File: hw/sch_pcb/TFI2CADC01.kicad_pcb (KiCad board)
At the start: 2 copper layers, 30 x 20 mm, 32 parts, among them J1 SM04B-GHS-TB, J2 SM04B-GHS-TB, J3 SM04B-GHS-TB, J4 SM04B-GHS-TB, J5 SM04B-GHS-TB, J6 SM04B-GHS-TB, U1 MIC5504-3.3YM5, U2 LTC4317

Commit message: Hotové schéma - otázka jumpery a konektory na vstupu
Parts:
- removed G1: LOGO, MLAB_LOGA:TF 10x4,7
- removed J6: SM04B-GHS-TB, Connector_JST:JST_GH_SM04B-GHS-TB_1x04-1MP_P1.25mm_Horizontal
- removed R10, R12, R15: 1M, Resistor_SMD:R_0603_1608Metric
- removed R13, R14, R9: 887k, Resistor_SMD:R_0603_1608Metric
- removed R16, R17: 10k, Resistor_SMD:R_0603_1608Metric
- removed R7: -, Resistor_SMD:R_0603_1608Metric
- removed R8: 180R, Resistor_SMD:R_0603_1608Metric
- removed U2: LTC4317, Package_DFN_QFN:DFN-16-1EP_3x5mm_P0.5mm_EP1.66x4.4mm
- added C5: 100nF, Capacitor_SMD:C_0603_1608Metric, F.Cu at (89.6, 104.2)
- added D3: LED RED, LED_SMD:LED_0603_1608Metric, F.Cu at (93.7, 111.0)
- added JP3: 0x4A, Jumper:SolderJumper-2_P1.3mm_Open_RoundedPad1.0x1.5mm, F.Cu at (85.4, 109.3)
- added JP4: 0x4B, Jumper:SolderJumper-2_P1.3mm_Open_RoundedPad1.0x1.5mm, F.Cu at (85.4, 112.9)
- added Q1: BC817, Package_TO_SOT_SMD:SOT-23, F.Cu at (94.1, 107.5)
- added R4: 10k, Resistor_SMD:R_0603_1608Metric, F.Cu at (89.6, 106.7)
- added U3: ADS1115IDGS, Package_SO:TSSOP-10_3x3mm_P0.5mm, F.Cu at (103.0, 108.2)
- C1, C2, C3, D1, D2, J3, R1, R2, R3, R5, U1: moved to F.Cu
- C4: value 100nF -> 10uF; moved to F.Cu
- J1: value SM04B-GHS-TB -> Screw_Terminal_01x06; footprint Connector_JST:JST_GH_SM04B-GHS-TB_1x04-1MP_P1.25mm_Horizontal -> TerminalBlock_Phoenix:TerminalBlock_Phoenix_PTSM-0,5-5-2,5-V-SMD_1x05-1MP_P2.50mm_Vertical; moved to F.Cu
- J2: value SM04B-GHS-TB -> ALERT/RDY; footprint Connector_JST:JST_GH_SM04B-GHS-TB_1x04-1MP_P1.25mm_Horizontal -> TestPoint:TestPoint_Keystone_5015_Micro_Mini; moved to F.Cu
- J5: value SM04B-GHS-TB -> Conn_01x06_Pin; footprint Connector_JST:JST_GH_SM04B-GHS-TB_1x04-1MP_P1.25mm_Horizontal -> Connector_PinHeader_2.54mm:PinHeader_1x06_P2.54mm_Horizontal; moved to F.Cu
- JP1: value SolderJumper_2_Open -> 0x48
- JP2: value SolderJumper_2_Open -> 0x49
- R6: value 10k -> 180R; moved to F.Cu
- moved C2 60.8 mm to (93.4, 80.6)
- moved C3 58.6 mm to (93.4, 83.1)
- moved JP1 57.6 mm to (85.4, 102.2), turned to 0 degrees
- moved JP2 57.6 mm to (85.4, 105.8), turned to 0 degrees
- moved R5 56.4 mm to (89.6, 109.2), turned to 0 degrees
- moved C4 55.1 mm to (89.6, 101.7), turned to 0 degrees
- moved R6 54.8 mm to (89.6, 111.7), turned to 0 degrees
- moved R1 50.2 mm to (93.4, 85.6), turned to 0 degrees
- moved R2 46.4 mm to (93.4, 88.1), turned to 0 degrees
- moved U1 46.1 mm to (96.4, 98.5), turned to 0 degrees
- moved D2 45.9 mm to (101.7, 80.7), turned to 0 degrees
- moved R3 44.3 mm to (93.4, 90.6), turned to 0 degrees
- moved J1 40.4 mm to (171.8, 105.0)
- moved J3 35.8 mm to (117.5, 94.0)
- moved J2 30.5 mm to (101.2, 102.3), turned to 0 degrees
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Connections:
- J1 pad 1: +5V -> unconnected-(J1-Pin_1-Pad1)
- J1 pad 2: /SCLin -> unconnected-(J1-Pin_2-Pad2)
- J1 pad 3: /SDAin -> unconnected-(J1-Pin_3-Pad3)
- J1 pad 4: GND -> unconnected-(J1-Pin_4-Pad4)
- J1 pad MP: GND -> (no net)
- J2 pad 1: +5V -> /ALERT/RDY
- J3 pad 2: /SCLout1 -> /SCL
- J3 pad 3: /SDAout1 -> /SDA
- J4 pad 2: /SCLout1 -> /SCL
- J4 pad 3: /SDAout1 -> /SDA
- J5 pad 1: +5V -> GND
- J5 pad 2: /SCLout2 -> /AIN3
- J5 pad 3: /SDAout2 -> /AIN2
- J5 pad 4: GND -> /AIN1
- JP1 pad 1: /XORL1 -> /ADDR
- JP1 pad 2: +3V3 -> GND
- JP2 pad 1: /XORL2 -> /ADDR
- R2 pad 2: /SCLin -> /SCL
- R3 pad 2: /SDAin -> /SDA
- R5 pad 1: +3V3 -> Net-(Q1-B)
- R5 pad 2: /SCLout1 -> /ALERT/RDY
- R6 pad 1: +3V3 -> +5V
- R6 pad 2: /SDAout1 -> Net-(D3-A)
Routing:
- net +5V: track 61.4 -> 0.00 mm, vias 3 -> 0
- net +3V3: track 56.3 -> 0.00 mm, vias 5 -> 0
- net /SDAin: track 22.5 -> 0.00 mm, vias 2 -> 0
- net /SCLin: track 20.5 -> 0.00 mm, vias 3 -> 0
- net /SCLout2: track 18.5 -> 0.00 mm, vias 3 -> 0
- net /SDAout2: track 18.1 -> 0.00 mm, vias 1 -> 0
- net /XORL1: track 17.4 -> 0.00 mm, vias 1 -> 0
- net /SDAout1: track 17.4 -> 0.00 mm, vias 1 -> 0
- net /SCLout1: track 16.2 -> 0.00 mm, vias 3 -> 0
- net /XORL2: track 12.4 -> 0.00 mm, vias 1 -> 0
- net /XORH1: track 9.16 -> 0.00 mm
- net /XORH2: track 6.98 -> 0.00 mm
- net GND: track 3.96 -> 0.00 mm, vias 26 -> 0
- net Net-(D1-A): track 2.50 -> 0.00 mm
- removed copper zone on B.Cu, net GND
- removed copper zone on F.Cu, net GND
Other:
- board size 30 x 20 mm -> 35 x 20 mm
- board text removed: "0x08 0x0f"
- board text removed: "0x78 0x7f"
- board text removed: "2023"
- board text removed: "I2C input (pass-trough)"
- board text removed: "OUT1"
- board text removed: "OUT2"
- board text removed: "TFI2CADT01B"
- board text removed: "thunderfly.cz"

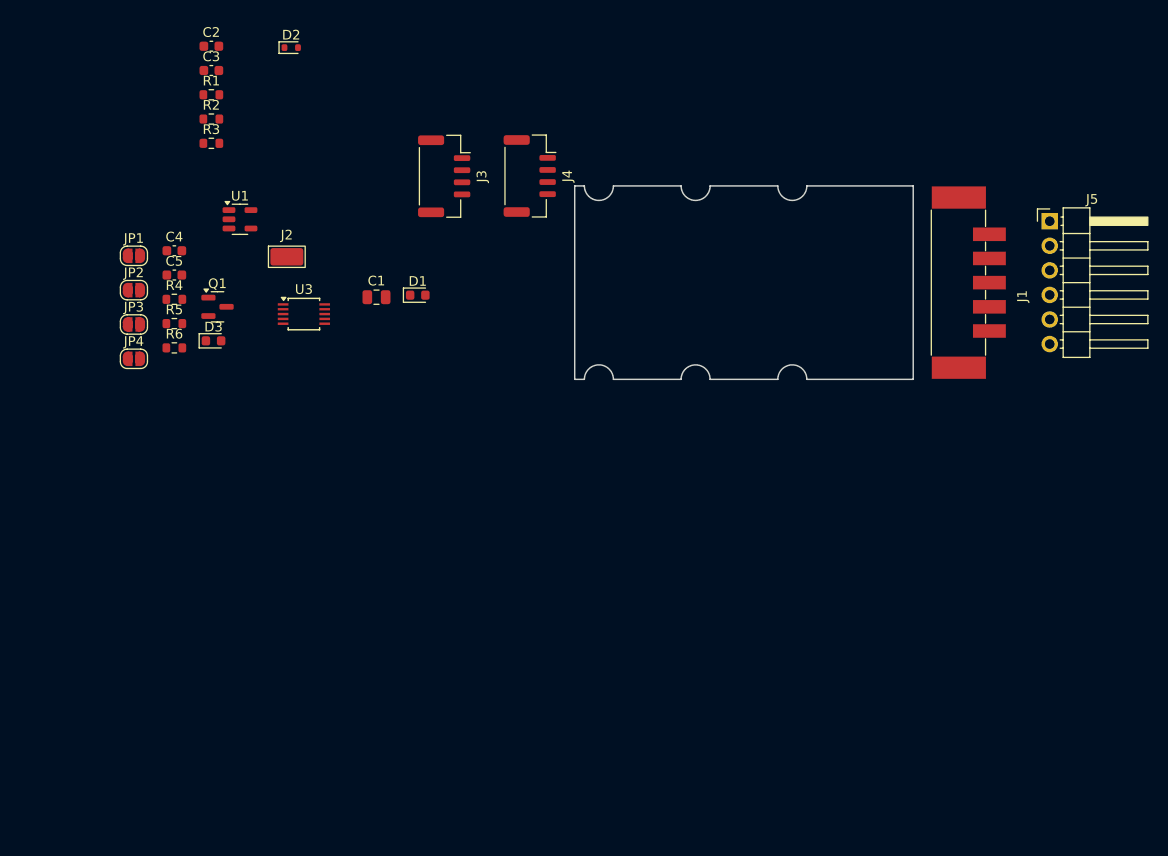
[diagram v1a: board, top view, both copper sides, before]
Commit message: ADS1115 obvod s headry
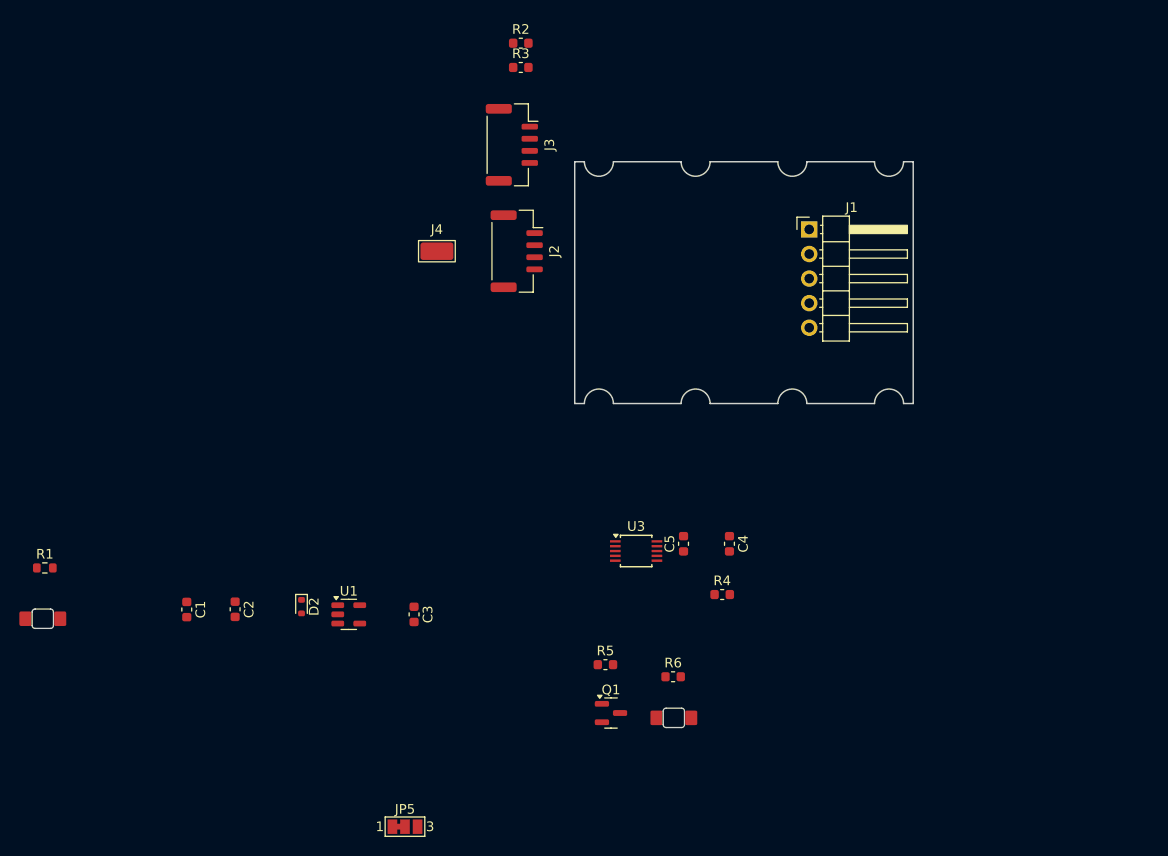
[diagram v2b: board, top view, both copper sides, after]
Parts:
- removed J5: Conn_01x06_Pin, Connector_PinHeader_2.54mm:PinHeader_1x06_P2.54mm_Horizontal
- removed JP1: 0x48, Jumper:SolderJumper-2_P1.3mm_Open_RoundedPad1.0x1.5mm
- removed JP2: 0x49, Jumper:SolderJumper-2_P1.3mm_Open_RoundedPad1.0x1.5mm
- removed JP3: 0x4A, Jumper:SolderJumper-2_P1.3mm_Open_RoundedPad1.0x1.5mm
- removed JP4: 0x4B, Jumper:SolderJumper-2_P1.3mm_Open_RoundedPad1.0x1.5mm
- added JP5: AddresSelect, Jumper:SolderJumper-3_P1.3mm_Bridged12_Pad1.0x1.5mm_NumberLabels, F.Cu at (113.5, 161.2)
- C1: footprint Capacitor_SMD:C_0805_2012Metric -> Mlab_R:SMD-0603
- C2, C3, C4, C5: footprint Capacitor_SMD:C_0603_1608Metric -> Mlab_R:SMD-0603
- D1, D3: footprint LED_SMD:LED_0603_1608Metric -> Mlab_D:LED_1206_mill
- J1: value Screw_Terminal_01x06 -> Conn_01x05_Pin; footprint TerminalBlock_Phoenix:TerminalBlock_Phoenix_PTSM-0,5-5-2,5-V-SMD_1x05-1MP_P2.50mm_Vertical -> Connector_PinHeader_2.54mm:PinHeader_1x05_P2.54mm_Horizontal
- R2, R3, R4, R5, R6: footprint Resistor_SMD:R_0603_1608Metric -> Mlab_R:SMD-0603
- moved C4 64.9 mm to (147.0, 132.0), turned to -90 degrees
- moved R4 64.3 mm to (146.2, 137.2)
- moved R6 61.8 mm to (141.2, 145.8)
- moved D3 61.5 mm to (141.2, 150.0)
- moved C3 60.0 mm to (114.4, 139.3), turned to -90 degrees
- moved C5 59.5 mm to (142.2, 132.0), turned to 90 degrees
- moved Q1 58.5 mm to (134.8, 149.5)
- moved C2 58.3 mm to (95.9, 138.8), turned to -90 degrees
- moved D2 57.8 mm to (102.8, 138.5), turned to -90 degrees
- moved R5 56.8 mm to (134.2, 144.5)
- moved R1 51.9 mm to (76.2, 134.5)
- moved D1 51.2 mm to (76.0, 139.8)
- moved U1 42.4 mm to (107.6, 139.3)
- moved U3 42.2 mm to (137.3, 132.8)
- moved C1 37.8 mm to (90.9, 138.8), turned to -90 degrees
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- renumbered J3 to J2, J4 to J3, J2 to J4
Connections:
- J1 pad 1: unconnected-(J1-Pin_1-Pad1) -> GND
- J1 pad 2: unconnected-(J1-Pin_2-Pad2) -> /AIN3
- J1 pad 3: unconnected-(J1-Pin_3-Pad3) -> /AIN2
- J1 pad 4: unconnected-(J1-Pin_4-Pad4) -> /AIN1
- J1 pad 5: unconnected-(J1-Pin_5-Pad5) -> /AIN0
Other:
- board size 35 x 20 mm -> 35 x 25 mm

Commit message: Updating footprints
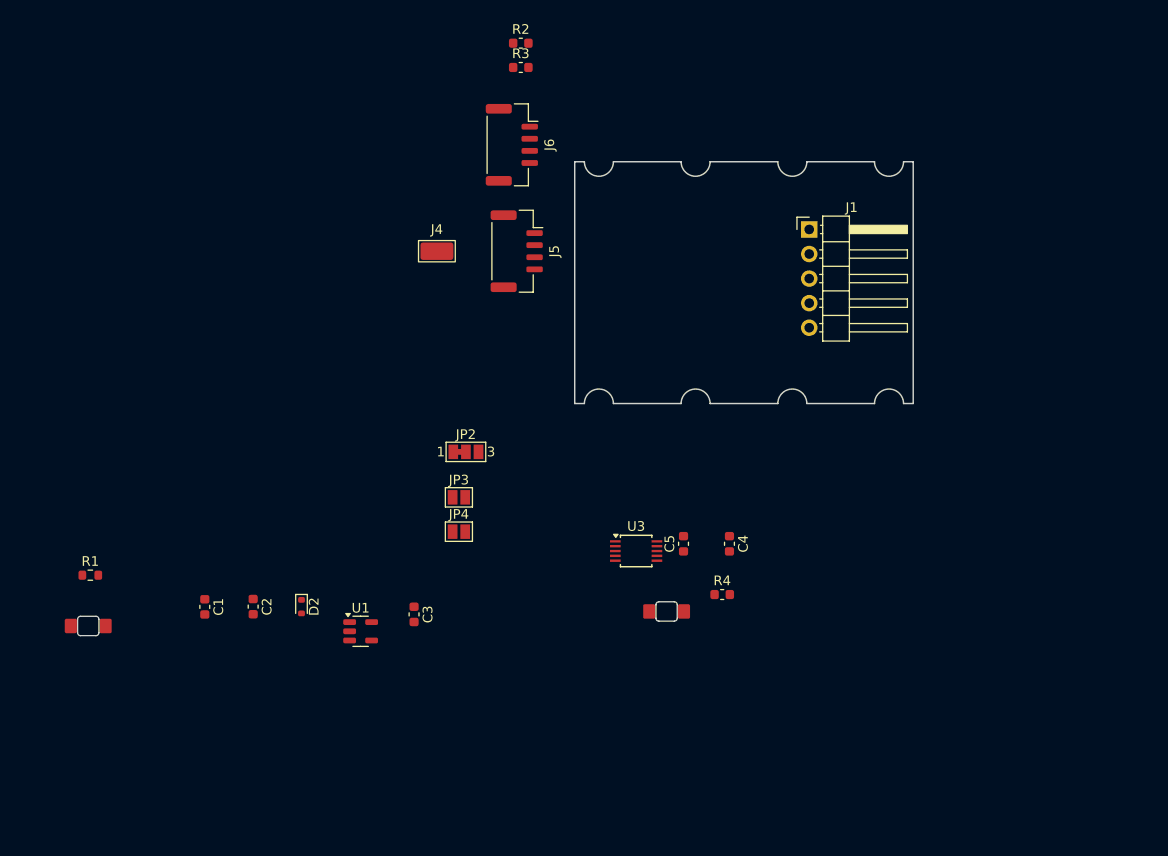
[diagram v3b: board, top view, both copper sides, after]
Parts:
- removed Q1: BC817, Package_TO_SOT_SMD:SOT-23
- removed R5: 10k, Mlab_R:SMD-0603
- removed R6: 180R, Mlab_R:SMD-0603
- added JP3: 0x4A, Jumper:SolderJumper-2_P1.3mm_Open_Pad1.0x1.5mm, F.Cu at (119.0, 127.2)
- added JP4: 0x4B, Jumper:SolderJumper-2_P1.3mm_Open_Pad1.0x1.5mm, F.Cu at (119.0, 130.8)
- D3: value LED RED -> LED ORANGE
- R4: value 10k -> 4k7
- moved JP2 39.3 mm to (119.8, 122.5)
- moved D3 11.0 mm to (140.5, 139.0)
- moved D1 4.76 mm to (80.7, 140.5)
- moved R1 4.76 mm to (80.9, 135.2)
- moved U1 2.14 mm to (108.9, 141.1)
- moved C1 1.88 mm to (92.8, 138.5)
- moved C2 1.88 mm to (97.8, 138.5)
- renumbered J2 to J5, J3 to J6, JP5 to JP2
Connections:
- D3 pad 1: Net-(D3-K) -> /ALERT/RDY
- JP2 pad 2: +3V3 -> GND
- JP2 pad 3: GND -> +3V3
- R4 pad 1: +3V3 -> Net-(D3-A)
- R4 pad 2: /ALERT/RDY -> +3V3

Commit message: Updating schematics
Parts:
- removed JP4: 0x4B, Jumper:SolderJumper-2_P1.3mm_Open_Pad1.0x1.5mm
- added JP1: ~, Jumper:SolderJumper-3_P1.3mm_Bridged12_Pad1.0x1.5mm_NumberLabels, F.Cu at (119.7, 119.2)
- JP2: value AddresSelect -> SolderJumper_2_Open; footprint Jumper:SolderJumper-3_P1.3mm_Bridged12_Pad1.0x1.5mm_NumberLabels -> Jumper:SolderJumper-2_P1.3mm_Open_Pad1.0x1.5mm
- JP3: value 0x4A -> SolderJumper_2_Open
- moved JP2 1.13 mm to (118.9, 123.2)
- moved JP3 0.42 mm to (118.9, 126.8)
- renumbered J4 to J2, J5 to J3, J6 to J4
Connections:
- JP2 pad 2: GND -> /SDA
- JP3 pad 2: /SDA -> /SCL

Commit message: Adding pcb
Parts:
- removed the C4 at (147.0, 132.0)
- removed the J3 at (125.0, 101.8)
- removed JP3: SolderJumper_2_Open, Jumper:SolderJumper-2_P1.3mm_Open_Pad1.0x1.5mm
- C1: footprint Mlab_R:SMD-0603 -> Mlab_R:SMD-0805
- D1: value LED GREEN -> PWR
- J1: value Conn_01x05_Pin -> HEADER_2x04; footprint Connector_PinHeader_2.54mm:PinHeader_1x05_P2.54mm_Horizontal -> Connector_PinHeader_2.54mm:PinHeader_2x04_P2.54mm_Edge_Mount
- J3: renamed from J4; moved to B.Cu
- JP1, JP2: moved to B.Cu
- T1: renamed from J2; moved to B.Cu
- moved D1 75.8 mm to (144.2, 99.2)
- moved R1 70.4 mm to (143.2, 102.5), turned to 90 degrees
- moved C1 65.2 mm to (147.0, 102.4), turned to 90 degrees
- moved C2 62.6 mm to (149.0, 102.5), turned to 90 degrees
- moved D2 55.5 mm to (145.1, 102.6), turned to 90 degrees
- moved U1 50.7 mm to (146.1, 106.6), turned to -90 degrees
- moved C3 47.6 mm to (148.9, 106.5)
- moved T1 39.3 mm to (155.4, 109.2)
- moved R2 36.6 mm to (155.6, 101.0), turned to -90 degrees
- moved R3 33.8 mm to (153.9, 101.0), turned to -90 degrees
- moved JP2 33.7 mm to (147.2, 105.0), turned to 90 degrees
- moved JP1 33.0 mm to (149.8, 105.6), turned to -90 degrees
- moved U2 32.0 mm to (154.5, 105.7), turned to 180 degrees
- moved R4 29.7 mm to (143.0, 107.8), turned to 90 degrees
- moved D3 28.5 mm to (144.2, 110.7)
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- renumbered C5 to C4, U3 to U2
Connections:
- J1 pad 2: /AIN3 -> GND
- J1 pad 3: /AIN2 -> /AIN1
- J1 pad 4: /AIN1 -> /AIN2
- JP1 pad 1: /ADDR -> GND
- JP1 pad 2: GND -> /ADDR
- JP2 pad 2: /SDA -> /SCL
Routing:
- net +3V3: track 0.00 -> 27.4 mm, vias 0 -> 1
- net /SCL: track 0.00 -> 25.6 mm, vias 0 -> 2
- net /SDA: track 0.00 -> 25.1 mm, vias 0 -> 2
- net +5V: track 0.00 -> 23.2 mm, vias 0 -> 1
- net /ALERT/RDY: track 0.00 -> 18.2 mm, vias 0 -> 1
- net /ADDR: track 0.00 -> 10.9 mm, vias 0 -> 1
- net /AIN2: track 0.00 -> 7.73 mm, vias 0 -> 1
- net /AIN3: track 0.00 -> 7.49 mm, vias 0 -> 1
- net GND: track 0.00 -> 5.12 mm, vias 0 -> 16
- net Net-(D3-A): track 0.00 -> 4.33 mm
- net /AIN0: track 0.00 -> 3.24 mm
- net /AIN1: track 0.00 -> 3.18 mm
- net Net-(D1-A): track 0.00 -> 2.91 mm
- added copper zone on B.Cu, net GND
- added copper zone on F.Cu, net GND
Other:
- board size 35 x 25 mm -> 25 x 15 mm
- board text added: "ALERT"
- board text added: "K"

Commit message: Adding pcb
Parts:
- added J2: SM04B-GHS-TB, Connector_JST:JST_GH_SM04B-GHS-TB_1x04-1MP_P1.25mm_Horizontal, F.Cu at (139.0, 105.0)
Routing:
- net GND: track 5.12 -> 3.92 mm

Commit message: Improve layout.
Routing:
- net /AIN3: track 7.49 -> 8.11 mm
- net GND: vias 16 -> 18
